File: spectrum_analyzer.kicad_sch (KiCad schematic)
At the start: 70 parts, among them J1 Arduino_Uno, Q1 PN2222A, Q2 PN2222A, Q3 PN2222A, Q4 PN2222A, Q5 PN2222A, Q6 PN2222A, U1 74HC595

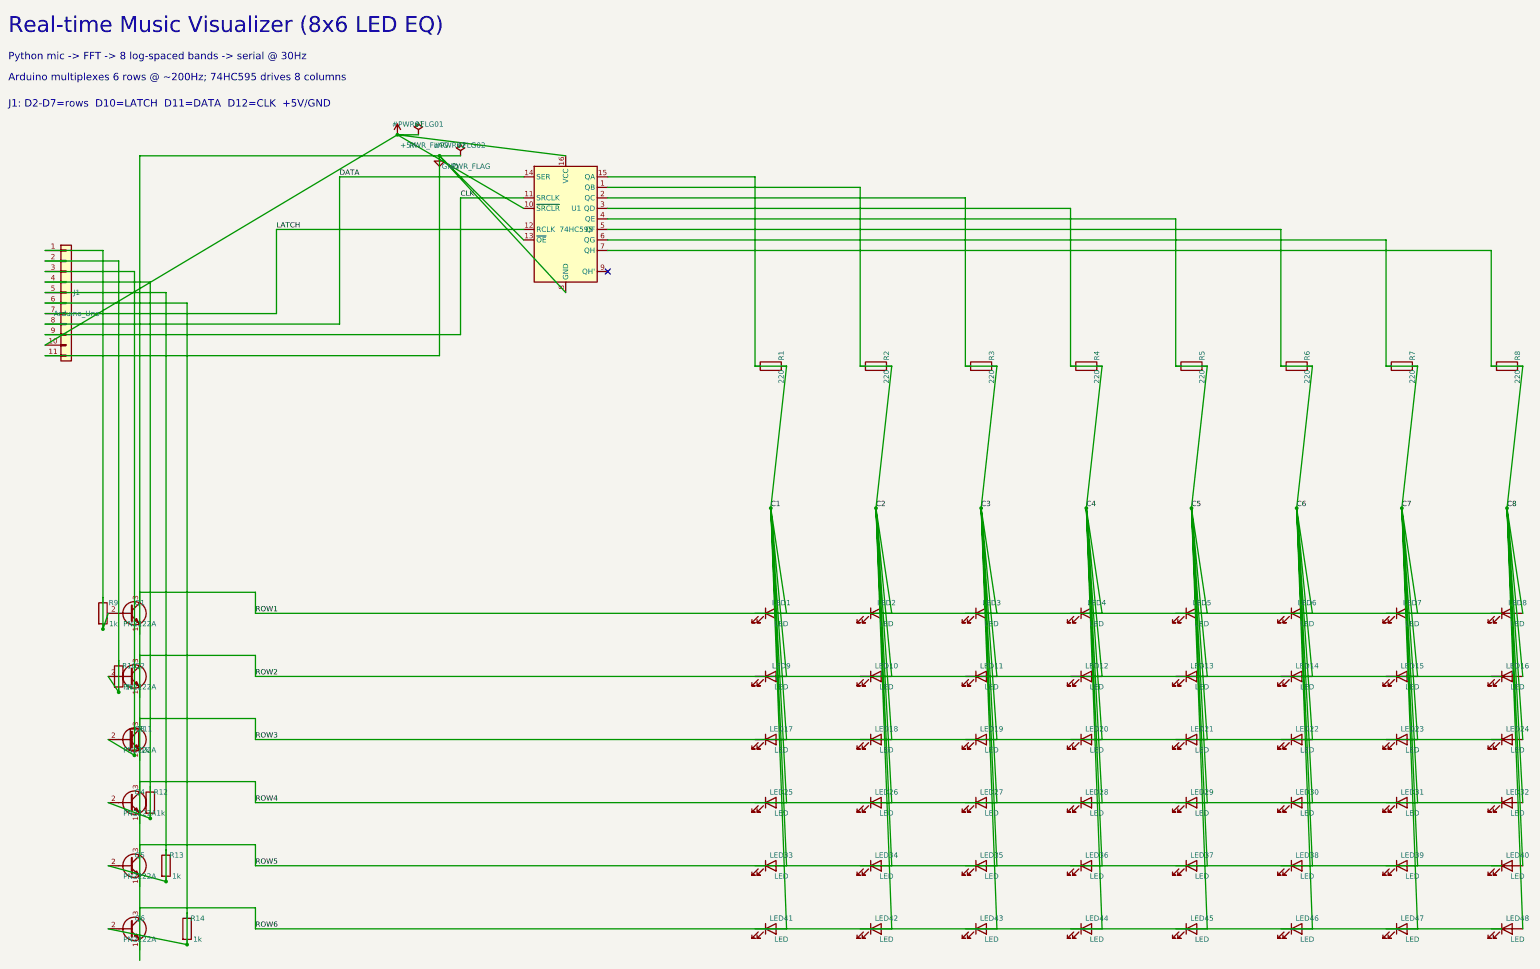
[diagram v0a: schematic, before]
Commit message: Rewrite schematic to match built 2x3 LED matrix visualizer
Regenerate the KiCad schematic to reflect the hardware actually built
(see README.md / music_visualizer.ino) instead of the original 8x6 design:

- 2 rows x 3 columns = 6 LEDs; 3x 220R column resistors, 2x 1k base resistors
- 74HC595 drives columns via Q1/Q2/Q3 (QB/QC/QD); Q0 and Q4-Q7 unused (no-connect)
- Correct control pin mapping: D10=SER/DATA, D11=RCLK/LATCH, D12=SRCLK/CLK
- 2x 2N2222 row sinks driven from D2/D3 through 1k base resistors
- Fix latent routing bugs inherited from the 8x6 version: resistors were shorted
  across both leads, and transistor emitters shorted to their collectors
- Strengthen netlist verification (series-resistor + per-node net checks) and
  emit a single ERC.rpt; ERC now passes with 0 errors / 0 warnings

Also refresh the BOM export and clear stale ERC debug reports/exclusions.

Co-authored-by: Cursor <cursoragent@cursor.com>
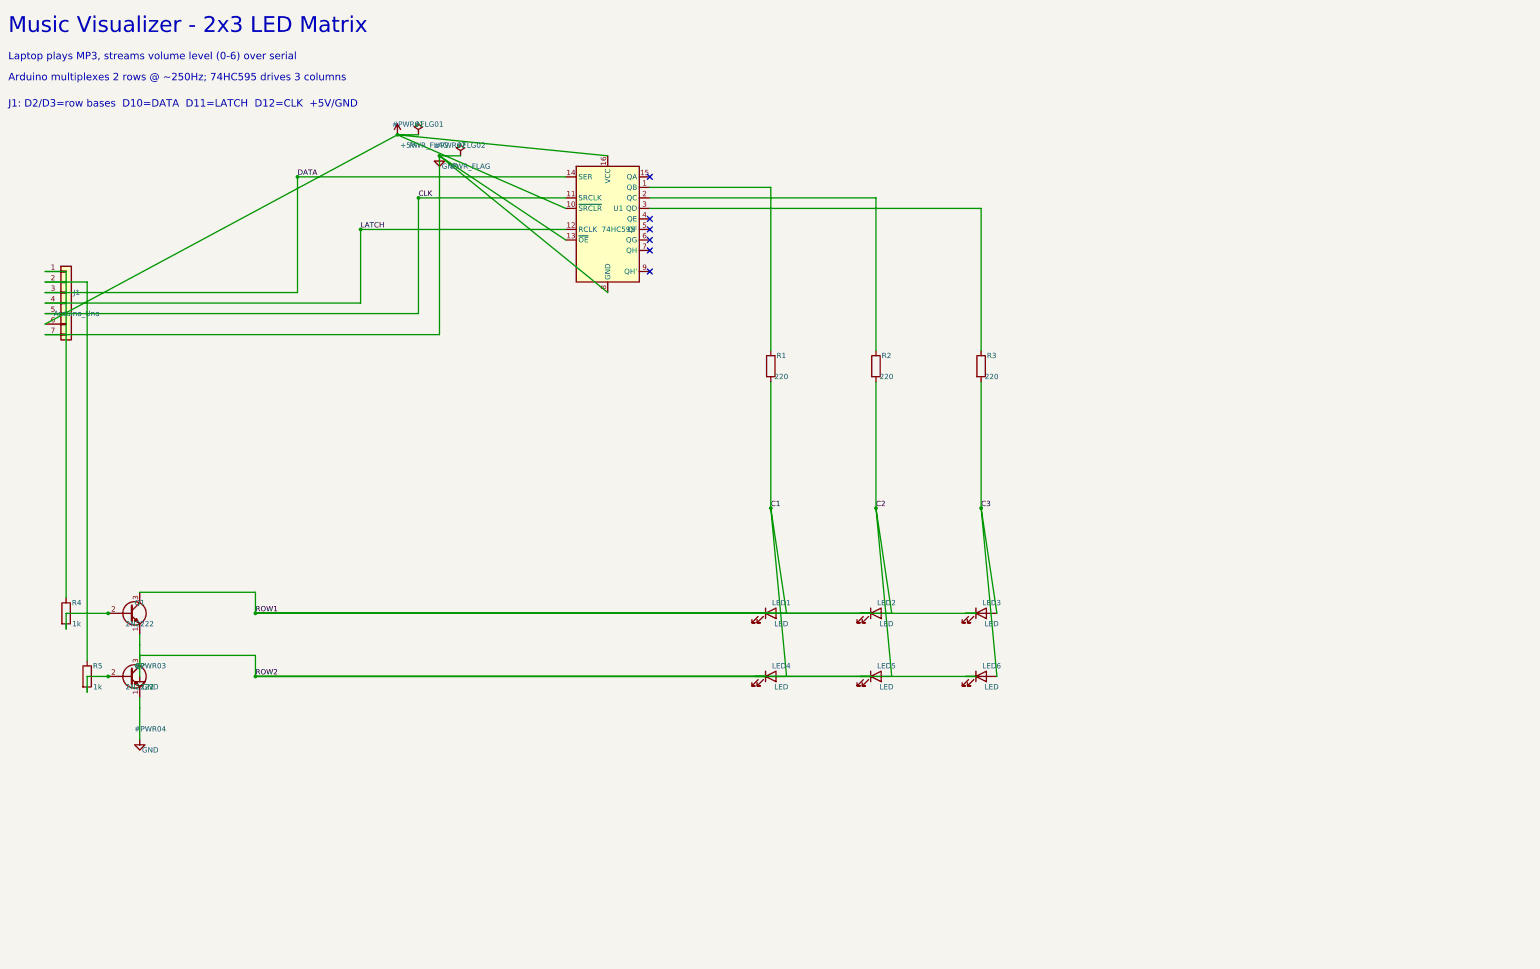
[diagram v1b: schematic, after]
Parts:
- removed J1: Arduino_Uno, Connector_PinHeader_2.54mm:PinHeader_1x11_P2.54mm_Vertical, symbol Connector_Generic:Conn_01x11
- removed LED10, LED11, LED12, LED13, LED14, LED15, LED16, LED17, LED18, LED19, LED20, LED21, LED22, LED23, LED24, LED25, LED26, LED27, LED28, LED29, LED30, LED31, LED32, LED33, LED34, LED35, LED36, LED37, LED38, LED39, LED40, LED41, LED42, LED43, LED44, LED45, LED46, LED47, LED48, LED7, LED8, LED9: LED, LED_THT:LED_D5.0mm, symbol Device:LED
- removed Q3, Q4, Q5, Q6: PN2222A, Package_TO_SOT_THT:TO-92_Inline, symbol Transistor_BJT:Q_NPN_EBC
- removed R10, R11, R12, R13, R14, R9: 1k, Resistor_THT:R_Axial_DIN0207_L6.3mm_D2.5mm_P10.16mm_Horizontal, symbol Device:R
- removed R6, R7, R8: 220, Resistor_THT:R_Axial_DIN0207_L6.3mm_D2.5mm_P10.16mm_Horizontal, symbol Device:R
- added J1: Arduino_Uno, Connector_PinHeader_2.54mm:PinHeader_1x07_P2.54mm_Vertical, symbol Connector_Generic:Conn_01x07
- Q1, Q2: value PN2222A -> 2N2222
- R1, R2, R3: footprint Resistor_THT:R_Axial_DIN0207_L6.3mm_D2.5mm_P10.16mm_Horizontal -> Resistor_THT:R_Axial_DIN0207_L6.3mm_D2.5mm_P5.08mm_Vertical
- R4, R5: value 220 -> 1k; footprint Resistor_THT:R_Axial_DIN0207_L6.3mm_D2.5mm_P10.16mm_Horizontal -> Resistor_THT:R_Axial_DIN0207_L6.3mm_D2.5mm_P5.08mm_Vertical
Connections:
- net +5V: now also J1.6 (Pin_6)
- net C1: now also LED4.2 (A); no longer R1.1, U1.15 (QA)
- net C2: now also LED5.2 (A); no longer R2.1, U1.1 (QB)
- net C3: now also LED6.2 (A); no longer R3.1, U1.2 (QC)
- net CLK: now also J1.5 (Pin_5)
- net DATA: now also J1.3 (Pin_3)
- net GND: now also Q1.1 (E), Q2.1 (E), J1.7 (Pin_7)
- net LATCH: now also J1.4 (Pin_4)
- net ROW1: now also LED1.1 (K), LED2.1 (K), LED3.1 (K)
- net ROW2: now also LED4.1 (K), LED5.1 (K), LED6.1 (K)
- net at Q1.2 (B): now also R4.2
- net at Q2.2 (B): now also R5.2
- removed net C4: LED4.2 (A), R4.1, R4.2, U1.3 (QD)
- removed net C5: LED5.2 (A), R5.1, R5.2, U1.4 (QE)
- net C6: no longer names the net of U1.5 (QF)
- net C6: no longer LED6.2 (A)
- net C7: no longer names the net of U1.6 (QG)
- net C8: no longer names the net of U1.7 (QH)
- new net: R1.1, U1.1 (QB)
- new net: R2.1, U1.2 (QC)
- new net: R3.1, U1.3 (QD)
- new net: J1.1 (Pin_1), R4.1
- new net: J1.2 (Pin_2), R5.1
- no-connect marks 1 -> 6
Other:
- note added: "Arduino multiplexes 2 rows @ ~250Hz; 74HC595 drives 3 columns"
- note added: "J1: D2/D3=row bases D10=DATA D11=LATCH D12=CLK +5V/GND"
- note added: "Laptop plays MP3, streams volume level (0-6) over serial"
- note added: "Music Visualizer - 2x3 LED Matrix"
- note removed: "Arduino multiplexes 6 rows @ ~200Hz; 74HC595 drives 8 columns"
- note removed: "J1: D2-D7=rows D10=LATCH D11=DATA D12=CLK +5V/GND"
- note removed: "Python mic -> FFT -> 8 log-spaced bands -> serial @ 30Hz"
- note removed: "Real-time Music Visualizer (8x6 LED EQ)"
- title: Spectrum Analyzer LED Matrix -> LED Matrix Music Visualizer (2x3)
